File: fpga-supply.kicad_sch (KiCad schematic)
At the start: 180 parts, among them J19 15910060, J20 15910060, U1 XC7K410T-2FFG900I

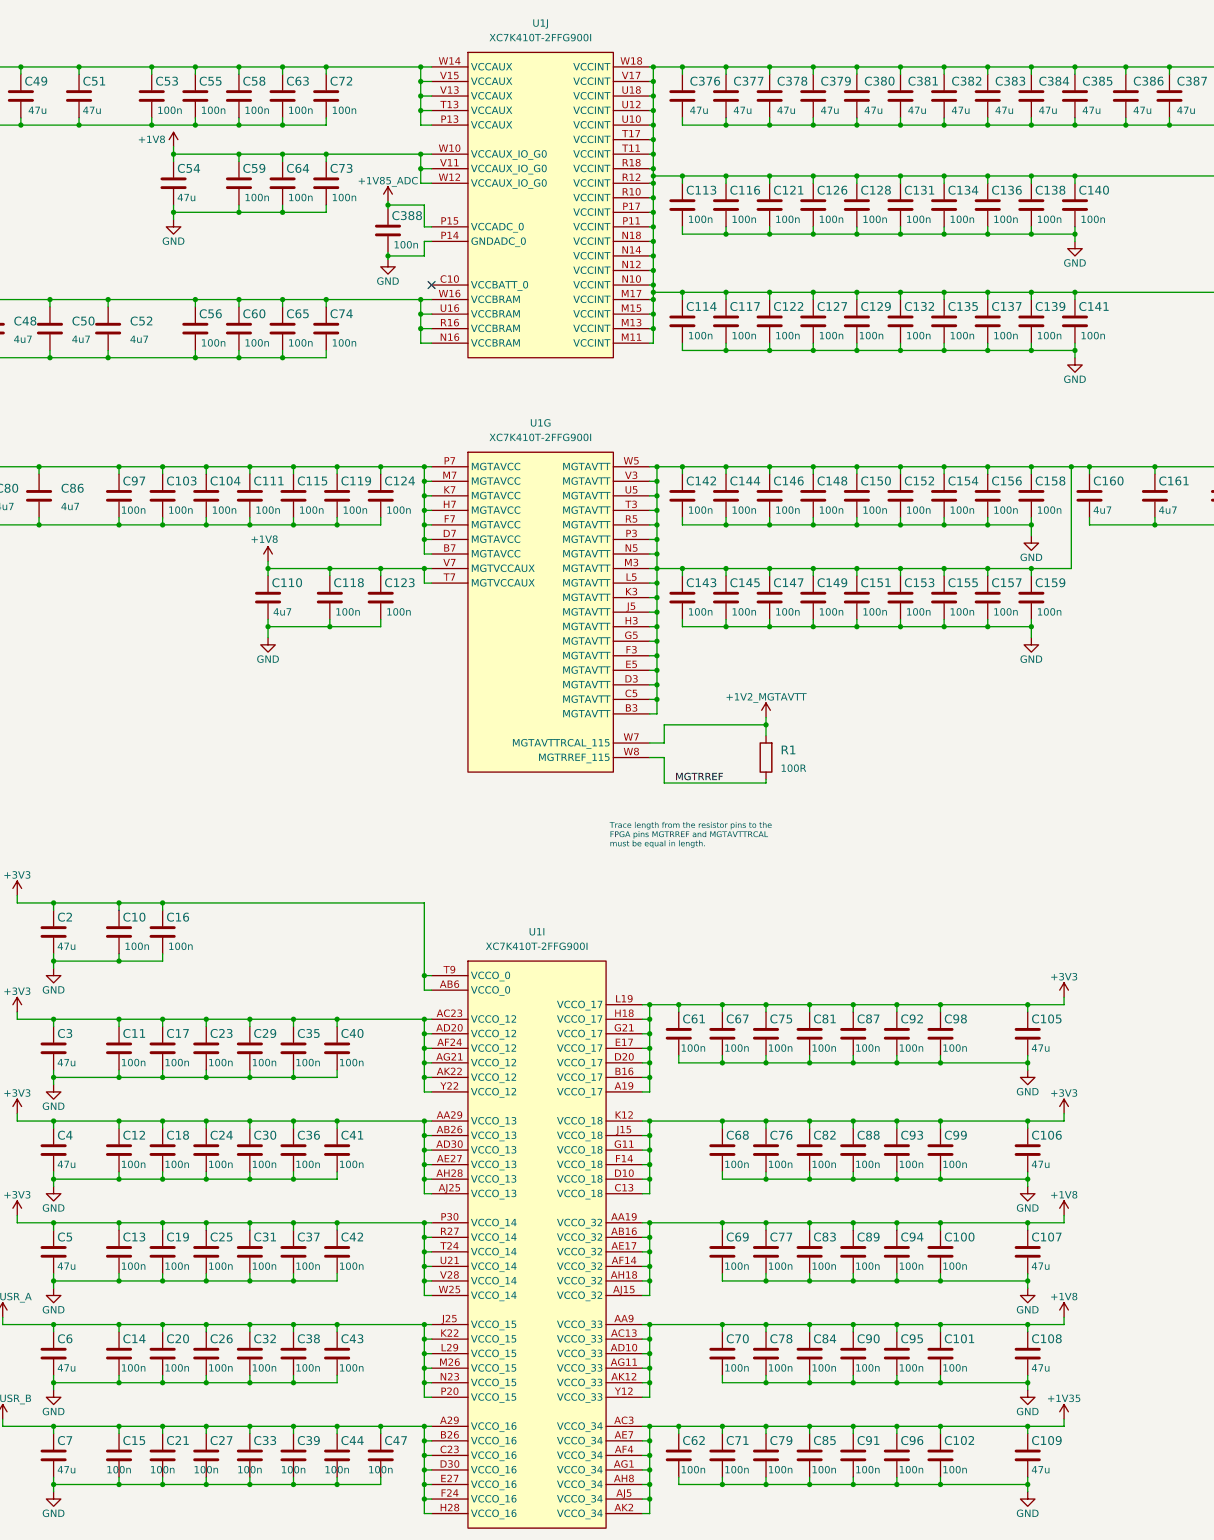
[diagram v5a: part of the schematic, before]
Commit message: Fix 100n value position
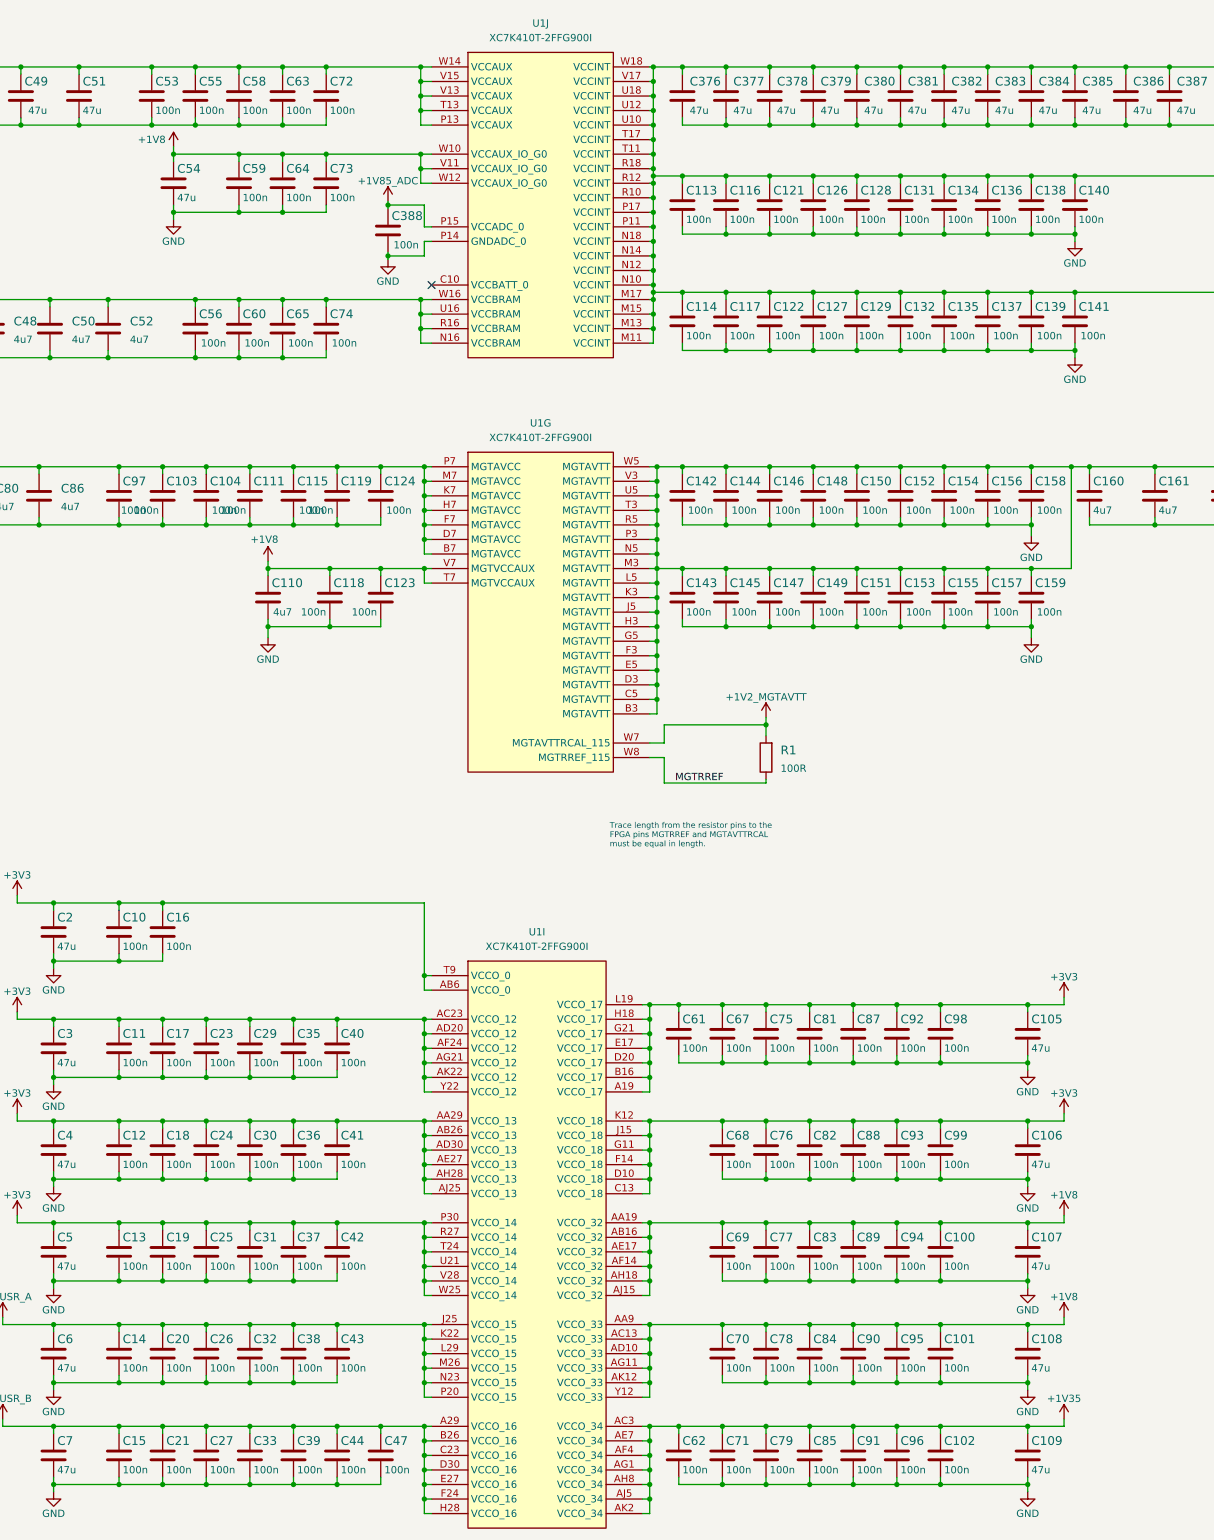
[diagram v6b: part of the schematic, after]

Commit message: Low speed routing
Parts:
- C110: value C_4u7_0402_EIA -> C_4u7_0201
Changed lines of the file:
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@@
       (effects (font (size 1.524 1.524)) (justify left))
     )
-    (property "Value" "C_4u7_0402_EIA" (id 1) (at 155.575 118.11 0)
+    (property "Value" "C_4u7_0201" (id 1) (at 155.575 118.11 0)
       (effects (font (size 1.524 1.524)) hide)
     )
